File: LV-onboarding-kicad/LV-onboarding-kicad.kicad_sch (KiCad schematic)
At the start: 33 parts, among them J2 AiM Sports Pressure Sensors X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, J3 HASS 50, U1 ${SIM.PARAMS}, U10 74AHC1G04, U11 74AHC1G04, U12 74AHC1G04, U13 74AHC1G04, U2A ${SIM.PARAMS}, U2B ${SIM.PARAMS}, U3 ${SIM.PARAMS}, U4 74AHC1G08, U5 74AHC1G08, U6 74AHC1G08, U6A ${SIM.PARAMS}, U6B ${SIM.PARAMS}, U7 74AHC1G08, U8 74AHC1G08

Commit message: BSPD research
rewatched vids from the goat ben eater for SR latch D latch and D flip flop. Added 74HC74 to schematic
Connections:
- net BSPD_TRIGGERED renamed SENSORS_TRIPPED
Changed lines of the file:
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@@
 		)
 	)
-	(global_label "BSPD_TRIGGERED"
+	(global_label "SENSORS_TRIPPED"
 		(shape input)
 		(at 180.34 93.98 0)
@@
 		)
 		(property "Intersheetrefs" "${INTERSHEET_REFS}"
-			(at 199.5327 93.98 0)
+			(at 200.8027 93.98 0)
 			(hide yes)
 			(show_name no)

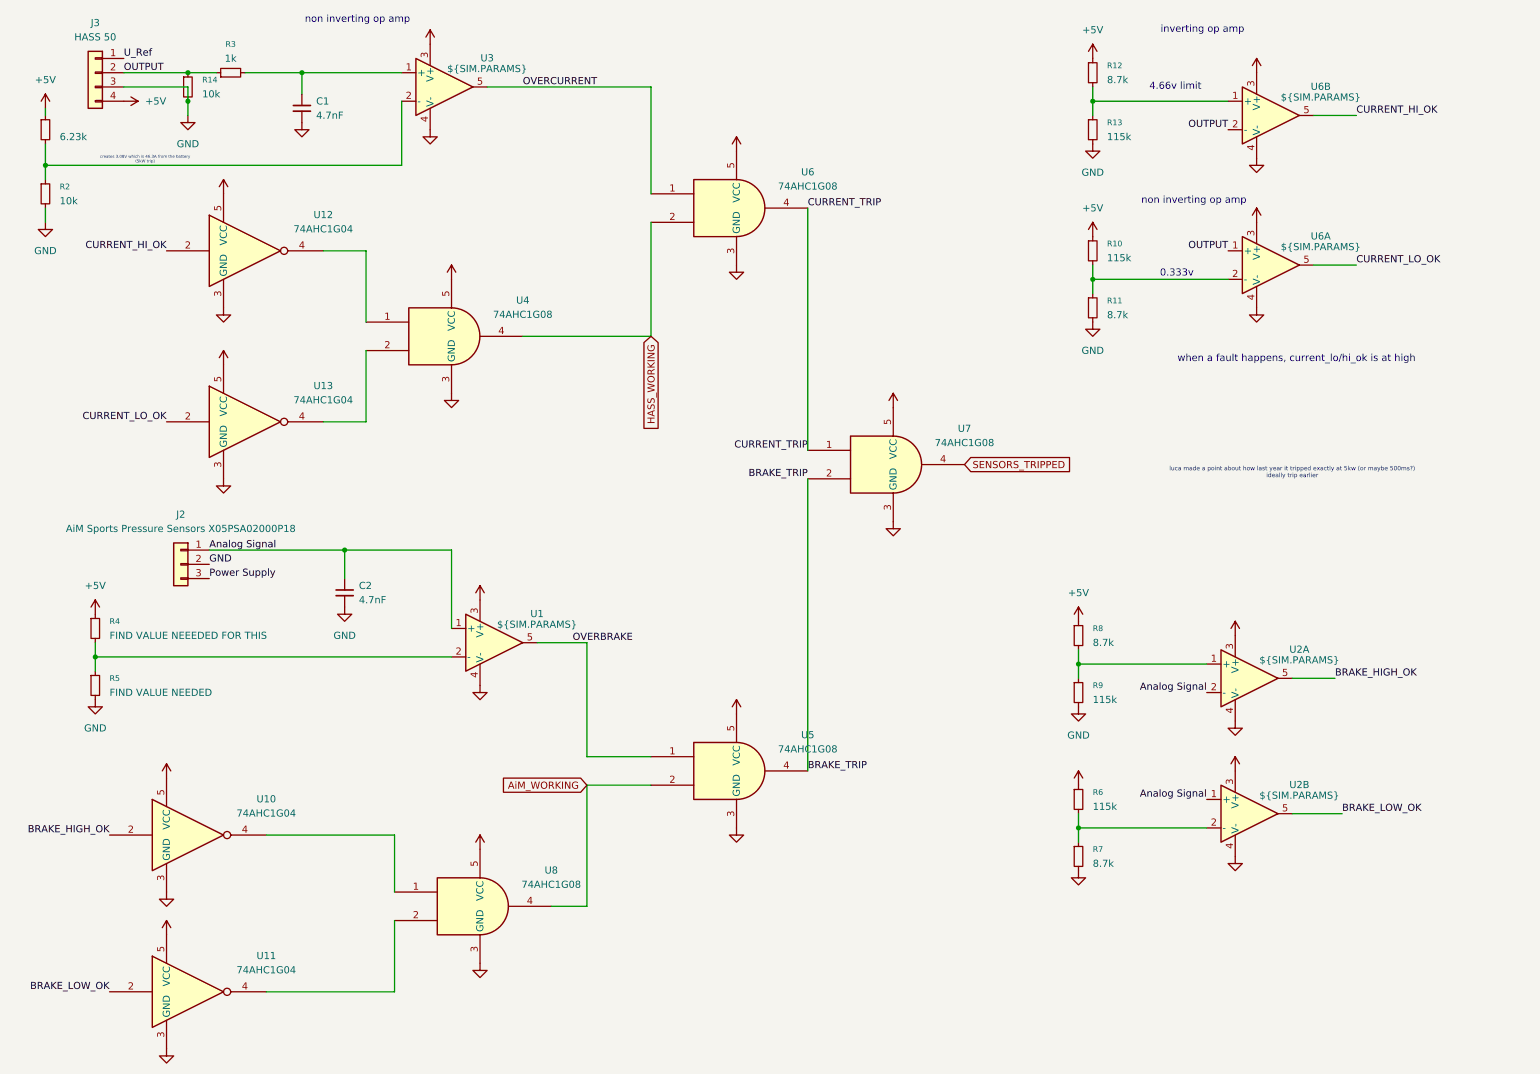
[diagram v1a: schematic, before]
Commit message: BSPD QOL changes
added delay block datasheet, cleaned up low and high thresholds on schematic, made SR latch, made +5v point up
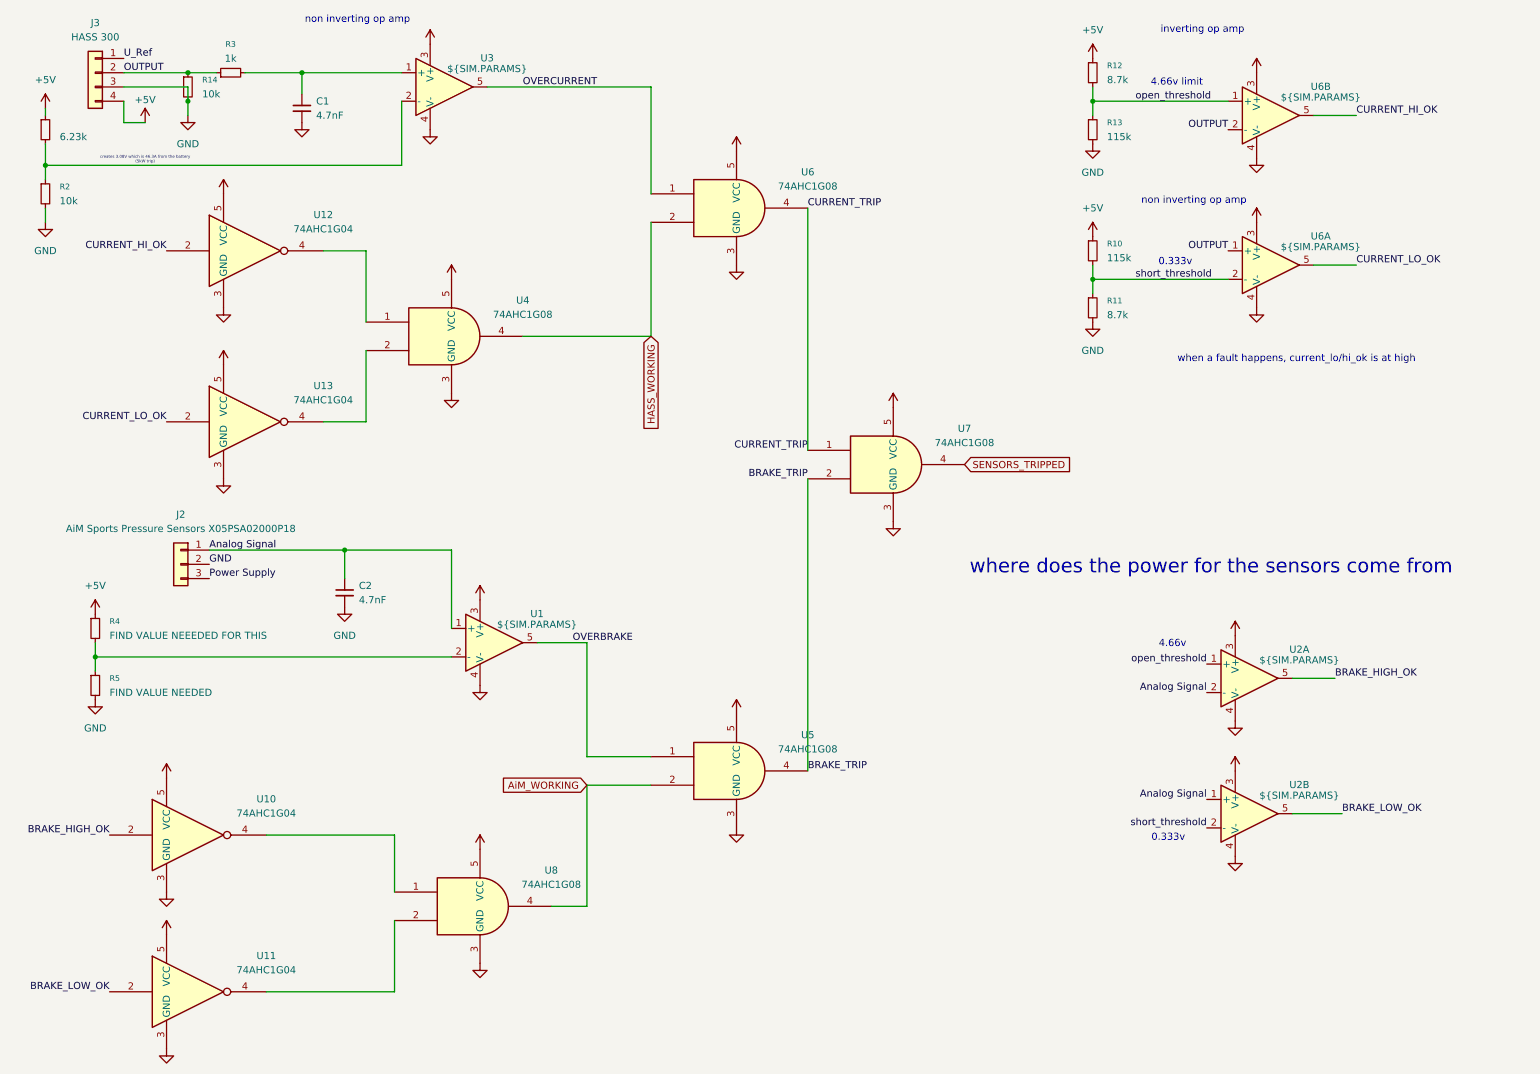
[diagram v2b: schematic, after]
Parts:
- removed R6, R9: 115k, symbol Device:R_Small
- removed R7, R8: 8.7k, symbol Device:R_Small
- J3: value HASS 50 -> HASS 300
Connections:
- net short_threshold: now reaches U2B.2 (-)
- net short_threshold: now also R10.2, R11.1, U6A.2 (-)
- net open_threshold: now reaches R12.2, R13.1, U6B.1 (+)
- net open_threshold: now also U2A.1 (+)
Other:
- note added: "4.66v"
- note added: "where does the power for the sensors come from"
- note removed: "luca made a point about how last year it tripped exactly at 5kw (or maybe 500ms?) ideally trip earlier"
